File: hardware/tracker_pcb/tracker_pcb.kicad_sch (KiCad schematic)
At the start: 0 parts

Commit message: Parts is parts
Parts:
- added H1, H2, H3, H4: MountingHole_Pad, MountingHole:MountingHole_3mm_Pad_TopBottom, symbol Mechanical:MountingHole_Pad
- added IC1, IC4: DRV8243HQRXYRQ1, footprint:DRV8243HQRXYRQ1, symbol symbol:DRV8243HQRXYRQ1
- added IC2: THVD1426DRLR, footprint:SOTFL50P160X60-8N, symbol symbol:THVD1426DRLR
- added IC3: TPS54302DDCR, SOT95P280X110-6N, symbol symbol:TPS54302DDCR
- added J1, J2, J3: 2601-1102, footprint:CONN2_2601-1102_WAG, symbol symbol:2601-1102
- added RJ1: RJ45 Shielded, footprint:RJ45-TH_R-RJ45R08P-B000, symbol symbol:R-RJ45R08P-B000
- added RJ2: ~, footprint:RJ45-TH_R-RJ45R08P-B000, symbol symbol:R-RJ45R08P-B000
- added U1: ESP32C6_SEEED, footprint:MODULE_113991054, symbol symbol:ESP32C6_SEEED

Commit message: WIP
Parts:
- removed IC3: TPS54302DDCR, SOT95P280X110-6N, symbol symbol:TPS54302DDCR
- removed J1, J2, J3: 2601-1102, footprint:CONN2_2601-1102_WAG, symbol symbol:2601-1102
- added C1, C6: 10uF, PCM_JLCPCB:C_1206, symbol Device:C
- added C2, C4: 100nF, PCM_JLCPCB:C_0603, symbol Device:C
- added C3: 33nF, PCM_JLCPCB:C_0603, symbol Device:C
- added C5: 47pF, PCM_JLCPCB:C_0603, symbol Device:C
- added D1: SS54, PCM_JLCPCB:D_SMA, symbol PCM_JLCPCB-Diodes:Schottky,SS54
- added J1: 256-406, footprint:WAGO_256-406, symbol symbol:256-406
- added JP?: SolderJumper_2_Open, symbol Jumper:SolderJumper_2_Open
- added L1: 4.7uH, footprint:IND-SMD_L12.3-W12.3, symbol Device:L
- added R1, R?: 21.5k, PCM_JLCPCB:R_0603, symbol Device:R_US
- added R2: 52.3k, PCM_JLCPCB:R_0603, symbol Device:R_US
- added R3: 10k, PCM_JLCPCB:R_0603, symbol Device:R_US
- added U2: TPS62933FDRLR, footprint:SOTFL50P160X60-8N, symbol symbol:TPS62933FDRLR
- added X2: 256-402, footprint:P-256-402, symbol symbol:256-402
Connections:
- net at IC1.14 (MODE): now also JP?.1 (A)
- net nSLEEP: now reaches IC1.3 (NSLEEP)
- net B+: now reaches IC1.4 (VM)
- net B+: now also C1.1, C2.1, D1.1, U2.3 (VIN)
- net at IC1.6 (GND): now also R?.1
- new net: C5.1, C6.1, L1.2, R2.2
- new net: R1.2, U2.1 (RT)
- new net: C4.2, L1.1, U2.5 (SW)
- new net: C4.1, U2.6 (BST)
- new net: C3.1, U2.7 (SS)
- new net: C5.2, R2.1, R3.2, U2.8 (FB)
- new net: JP?.2 (B), R?.2
- new net: D1.2, X2.L1.1, X2.L1.2
- new net GND: C1.2, C2.2, C3.2, C6.2, R1.1, R3.1, U2.4 (GND), X2.L2.1, X2.L2.2
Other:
- moved on the sheet: IC1, IC4

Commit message: wip
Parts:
- removed IC4: DRV8243HQRXYRQ1, footprint:DRV8243HQRXYRQ1, symbol symbol:DRV8243HQRXYRQ1
- added C1, C10, C2, C7, C8, C9: 100nF, PCM_JLCPCB:C_0603, symbol Device:C
- added C3, C4: 470uF, symbol Device:C_Polarized
- added JP2: SolderJumper_2_Open, symbol Jumper:SolderJumper_2_Open
- added R3: 21.5k, PCM_JLCPCB:R_0603, symbol Device:R_US
- added U2: DRV8243HQRXYRQ1, DRV8243HQRXYRQ1, symbol symbol:DRV8243HQRXYRQ1
- U1: renamed from IC1; footprint footprint:DRV8243HQRXYRQ1 -> DRV8243HQRXYRQ1
- gave numbers to parts that had none: 2
- renumbered C3 to C11, C4 to C12, C5 to C13, C6 to C14, C1 to C5, C2 to C6, IC2 to IC1, R2 to R4, R3 to R5, U2 to U3, U1 to U4, X2 to X1
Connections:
- net B+: now also C1.1, C2.1, C3.1, C4.1, U2.4 (VM)
- net GND: now also J1.2_1 (2), J1.2_2 (2__1), J1.5_1 (5), J1.5_2 (5__1), R2.1, U1.2 (IPROPI), U1.6 (GND), U1.8 (DRVOFF), C1.2, C10.2, C2.2, C3.2, C4.2, C7.2, C8.2, C9.2, R3.1, U2.2 (IPROPI), U2.6 (GND), U2.8 (DRVOFF)
- net nSLEEP: now also U2.3 (NSLEEP)
- net at R2.2: now also JP1.1 (A); no longer JP1.2 (B)
- net at U1.14 (MODE): now also JP1.2 (B); no longer JP1.1 (A)
- net M1_2: now reaches U1.5 (OUT2)
- net M1_2: now also J1.1_1 (1), J1.1_2 (1__1), C7.1
- net M1_1: now reaches U1.7 (OUT1)
- net M1_1: now also J1.3_1 (3), J1.3_2 (3__1), C9.1
- net M2_2: now reaches J1.4_1 (4)
- net M2_2: now also J1.4_2 (4__1), C8.1, U2.5 (OUT2)
- net M2_1: now reaches J1.6_1 (6)
- net M2_1: now also J1.6_2 (6__1), C10.1, U2.7 (OUT1)
- new net: JP2.2 (B), U2.14 (MODE)
- new net: JP2.1 (A), R3.2
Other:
- note added: "Solder jumper for half bridge ode"
- note added: "jump for half bridge mode"
- moved on the sheet: IC1, J1, JP1, R2, U1

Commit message: Adding 8244 models
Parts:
- added IC2: DRV8244HQRYJRQ1, footprint:DRV8244HQRYJRQ1, symbol symbol:DRV8244HQRYJRQ1
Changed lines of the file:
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@@
+	)
+	(symbol
+		(lib_id "symbol:DRV8244HQRYJRQ1")
+		(at 106.68 124.46 0)
+		(unit 1)
+		(exclude_from_sim no)
+		(in_bom yes)
+		(on_board yes)
+		(dnp no)
+		(fields_autoplaced yes)
+		(property "Reference" "IC2"
+			(at 125.3333 116.84 0)
+			(effects
+				(font
+					(size 1.27 1.27)
+				)
+				(justify left)
+			)
+		)
+		(property "Value" "DRV8244HQRYJRQ1"
+			(at 125.3333 119.38 0)
+			(effects
+				(font
+					(size 1.27 1.27)
+				)
+				(justify left)
+			)
+		)
+		(property "Footprint" "footprint:DRV8244HQRYJRQ1"
+			(at 135.89 219.38 0)
+			(effects
+				(font
+					(size 1.27 1.27)
+				)
+				(justify left top)
+				(hide yes)
+			)
+		)
+		(property "Datasheet" "https://www.ti.com/lit/ds/symlink/drv8244-q1.pdf?HQS=dis-mous-null-mousermode-dsf-pf-null-wwe"
+			(at 135.89 319.38 0)
+			(effects
+				(font
+					(size 1.27 1.27)
+				)
+				(justify left top)
+				(hide yes)
+			)
+		)
+		(property "Description" "Motor / Motion / Ignition Controllers & Drivers Automotive 40-V, 21-A H-Bridge driver with integrated current sensing and feedback 16-VQFN-HR -40 to 125"
+			(at 106.68 124.46 0)
+			(effects
+				(font
+					(size 1.27 1.27)
+				)
+				(hide yes)
+			)
+		)
+		(property "Height" ""
+			(at 135.89 519.38 0)
+			(effects
+				(font
+					(size 1.27 1.27)
+				)
+				(justify left top)
+				(hide yes)
+			)
+		)
+		(property "Mouser Part Number" "595-DRV8244HQRYJRQ1"
+			(at 135.89 619.38 0)
+			(effects
+				(font
+					(size 1.27 1.27)
+				)
+				(justify left top)
+				(hide yes)
+			)
+		)
+		(property "Mouser Price/Stock" "https://www.mouser.co.uk/ProductDetail/Texas-Instruments/DRV8244HQRYJRQ1?qs=Y0Uzf4wQF3nQ8wZEjQlEyg%3D%3D"
+			(at 135.89 719.38 0)
+			(effects
+				(font
+					(size 1.27 1.27)
+				)
+				(justify left top)
+				(hide yes)
+			)
+		)
+		(property "Manufacturer_Name" "Texas Instruments"
+			(at 135.89 819.38 0)
+			(effects
+				(font
+					(size 1.27 1.27)
+				)
+				(justify left top)
+				(hide yes)
+			)
+		)
+		(property "Manufacturer_Part_Number" "DRV8244HQRYJRQ1"
+			(at 135.89 919.38 0)
+			(effects
+				(font
+					(size 1.27 1.27)
+				)
+				(justify left top)
+				(hide yes)
+			)
+		)
+		(pin "2"
+		)
+		(pin "15"
+		)
+		(pin "11"
+		)
+		(pin "12"
+		)
+		(pin "5"
+		)
+		(pin "6"
+		)
+		(pin "10"
+		)
+		(pin "13"
+		)
+		(pin "14"
+		)
+		(pin "3"
+		)
+		(pin "16"
+		)
+		(pin "1"
+		)
+		(pin "4"
+		)
+		(pin "7"
+		)
+		(pin "8"
+		)
+		(pin "9"
+		)
+		(instances
+			(project ""
+				(path "/6aaa9514-f94e-4843-90d0-16960e4e49cb"
+					(reference "IC2")
+					(unit 1)
+				)
+			)
+		)
 	)
 	(symbol

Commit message: wip
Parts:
- removed U1: DRV8243HQRXYRQ1, DRV8243HQRXYRQ1, symbol symbol:DRV8243HQRXYRQ1
- IC2: footprint footprint:DRV8244HQRYJRQ1 -> DRV8244HQRYJRQ1
- L1: footprint footprint:IND-SMD_L12.3-W12.3 -> Inductor_SMD:L_10.4x10.4_H4.8
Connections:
- net B+: now also IC2.4 (VM)
- net GND: now also IC2.10 (DRVOFF), IC2.2 (IPROPI), IC2.7 (GND)
- net M1_1: now also IC2.8 (OUT1_1), IC2.9 (OUT1_2)
- net M1_2: now also IC2.5 (OUT2_1), IC2.6 (OUT2_2)
- net nSLEEP: now also IC2.3 (NSLEEP)
- net at JP1.2 (B): now also IC2.16 (MODE)
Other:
- moved on the sheet: IC2, JP1, R2

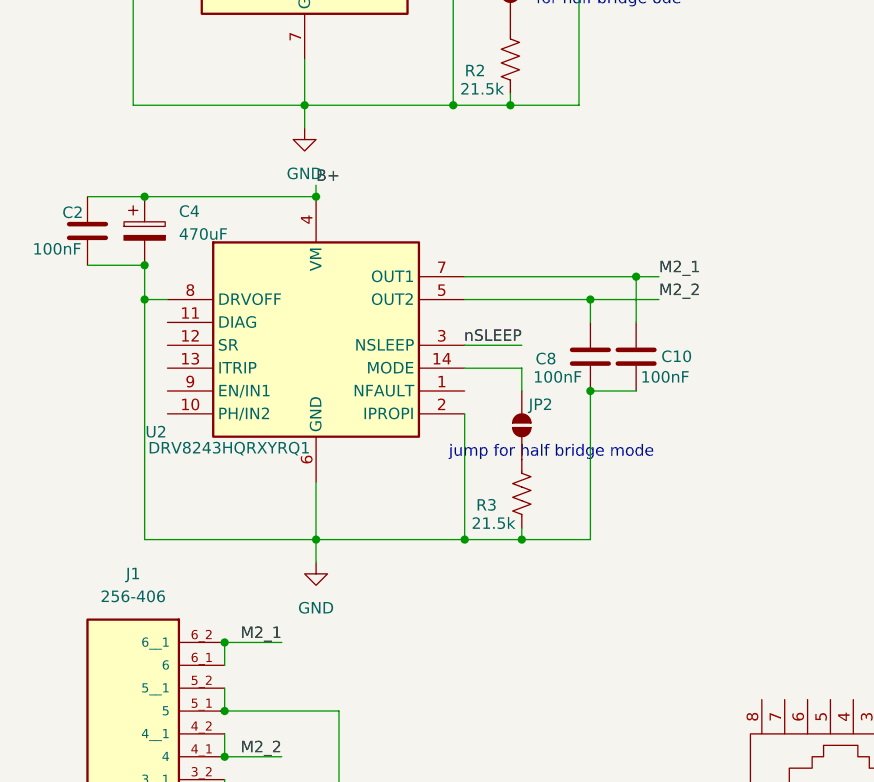
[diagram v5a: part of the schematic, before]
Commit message: Adding motor caps
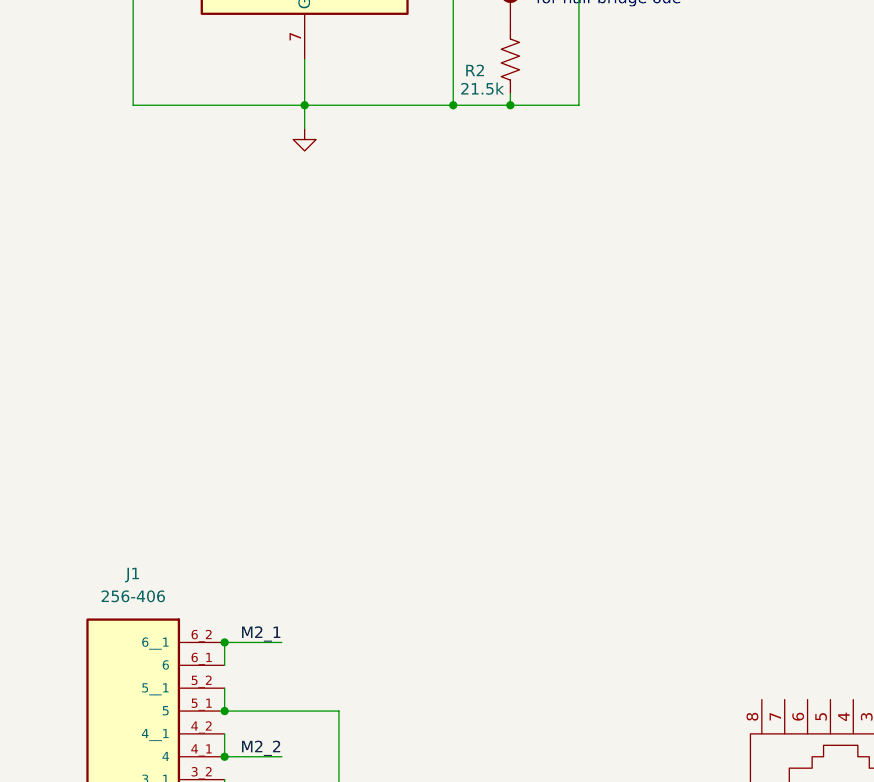
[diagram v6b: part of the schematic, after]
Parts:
- removed C10, C2, C8: 100nF, PCM_JLCPCB:C_0603, symbol Device:C
- removed C4: 470uF, symbol Device:C_Polarized
- removed JP2: SolderJumper_2_Open, symbol Jumper:SolderJumper_2_Open
- removed R3: 21.5k, PCM_JLCPCB:R_0603, symbol Device:R_US
- removed U2: DRV8243HQRXYRQ1, DRV8243HQRXYRQ1, symbol symbol:DRV8243HQRXYRQ1
- C3: footprint (none) -> Capacitor_SMD:CP_Elec_10x12.5
- IC2: footprint DRV8244HQRYJRQ1 -> footprint:DRV8244HQRYJRQ1
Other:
- note removed: "jump for half bridge mode"

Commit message: Routing begins
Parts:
- added C1, C7, C9: 100nF, Capacitor_SMD:C_0603_1608Metric, symbol Device:C
- added C3: 470uF, Capacitor_SMD:CP_Elec_10x12.5, symbol Device:C_Polarized
- added IC1: DRV8244HQRYJRQ1, footprint:DRV8244HQRYJRQ1, symbol symbol:DRV8244HQRYJRQ1
- added JP1: SolderJumper_2_Open, Resistor_SMD:R_0402_1005Metric_Pad0.72x0.64mm_HandSolder, symbol Jumper:SolderJumper_2_Open
- added R2: 21.5k, Resistor_SMD:R_0603_1608Metric, symbol Device:R_US
- C10: renamed from C9; footprint PCM_JLCPCB:C_0603 -> Capacitor_SMD:C_0603_1608Metric
- C11, C12, C13, C6: footprint PCM_JLCPCB:C_0603 -> Capacitor_SMD:C_0603_1608Metric
- C14: footprint PCM_JLCPCB:C_1206 -> Capacitor_SMD:C_0603_1608Metric
- C2: renamed from C1; footprint PCM_JLCPCB:C_0603 -> Capacitor_SMD:C_0603_1608Metric
- C5: footprint PCM_JLCPCB:C_1206 -> Capacitor_SMD:C_1206_3216Metric
- C8: renamed from C7; footprint PCM_JLCPCB:C_0603 -> Capacitor_SMD:C_0603_1608Metric
- D1: footprint PCM_JLCPCB:D_SMA -> Diode_SMD:D_SMA
- JP2: renamed from JP1; footprint (none) -> Resistor_SMD:R_0402_1005Metric_Pad0.72x0.64mm_HandSolder
- L1: footprint Inductor_SMD:L_10.4x10.4_H4.8 -> Inductor_SMD:L_12x12mm_H6mm
- R1, R4, R5: footprint PCM_JLCPCB:R_0603 -> Resistor_SMD:R_0603_1608Metric
- R3: renamed from R2; footprint PCM_JLCPCB:R_0603 -> Resistor_SMD:R_0603_1608Metric
- renumbered C3 to C4, IC1 to IC3, U3 to U1, U4 to U2
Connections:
- net GND: now also X1.L1.2, C1.2, C3.2, C7.2, C9.2, IC1.10 (DRVOFF), IC1.2 (IPROPI), IC1.7 (GND), R2.1; no longer X1.L2.1, X1.L2.2
- net M2_1: now also C9.1, IC1.8 (OUT1_1), IC1.9 (OUT1_2)
- net M2_2: now also C7.1, IC1.5 (OUT2_1), IC1.6 (OUT2_2)
- net nSLEEP: now also U2.5 (D4), IC1.3 (NSLEEP)
- net VDD: now reaches C13.1, C14.1, L1.2, R4.2
- net PWM1_F: now reaches U2.1 (D0)
- net PWM1_F: now also IC2.11 (EN/IN1)
- net PWM1_R: now reaches U2.2 (D1)
- net PWM1_R: now also IC2.12 (PH/IN2)
- net PWM2_F: now reaches U2.3 (D2)
- net PWM2_F: now also IC1.11 (EN/IN1)
- net PWM2_R: now reaches U2.4 (D3)
- net PWM2_R: now also IC1.12 (PH/IN2)
- net B+ renamed VIN
- net VIN: now also C1.1, C3.1, IC1.4 (VM)
- new net: D1.2, X1.L2.2
- new net: JP1.1 (A), R2.2
- new net: IC1.16 (MODE), JP1.2 (B)
- now unconnected: X1.L1.1
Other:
- moved on the sheet: X1

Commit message: More layout
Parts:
- H1, H2, H3, H4: footprint MountingHole:MountingHole_3mm_Pad_TopBottom -> MountingHole:MountingHole_3.5mm_Pad_Via
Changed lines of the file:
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@@
 			)
 		)
-		(property "Footprint" "MountingHole:MountingHole_3mm_Pad_TopBottom"
+		(property "Footprint" "MountingHole:MountingHole_3.5mm_Pad_Via"
 			(at 246.38 161.29 0)
 			(effects
@@
 			)
 		)
-		(property "Footprint" "MountingHole:MountingHole_3mm_Pad_TopBottom"
+		(property "Footprint" "MountingHole:MountingHole_3.5mm_Pad_Via"
 			(at 256.54 161.29 0)
 			(effects
@@
 			)
 		)
-		(property "Footprint" "MountingHole:MountingHole_3mm_Pad_TopBottom"
+		(property "Footprint" "MountingHole:MountingHole_3.5mm_Pad_Via"
 			(at 261.62 161.29 0)
 			(effects
@@
 			)
 		)
-		(property "Footprint" "MountingHole:MountingHole_3mm_Pad_TopBottom"
+		(property "Footprint" "MountingHole:MountingHole_3.5mm_Pad_Via"
 			(at 251.46 161.29 0)
 			(effects
